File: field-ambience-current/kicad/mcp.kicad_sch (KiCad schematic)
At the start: 17 parts, among them SW1 Cell 1 (2u Choc V2 Hot-Swap), SW10 Modifier CLEAR (1u Choc V2 Ho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, SW2 Cell 2 (2u Choc V2 Hot-Swap), SW3 Cell 3 (2u Choc V2 Hot-Swap), SW4 Cell 4 (2u Choc V2 Hot-Swap), SW5 Cell 5 (2u Choc V2 Hot-Swap), SW6 Modifier SHIFT (1u Choc V2 Ho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, SW7 Modifier HOLD (1u Choc V2 Hot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, SW8 Modifier DRONE (1u Choc V2 Ho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, SW9 Modifier GENERATE (1u Choc V2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

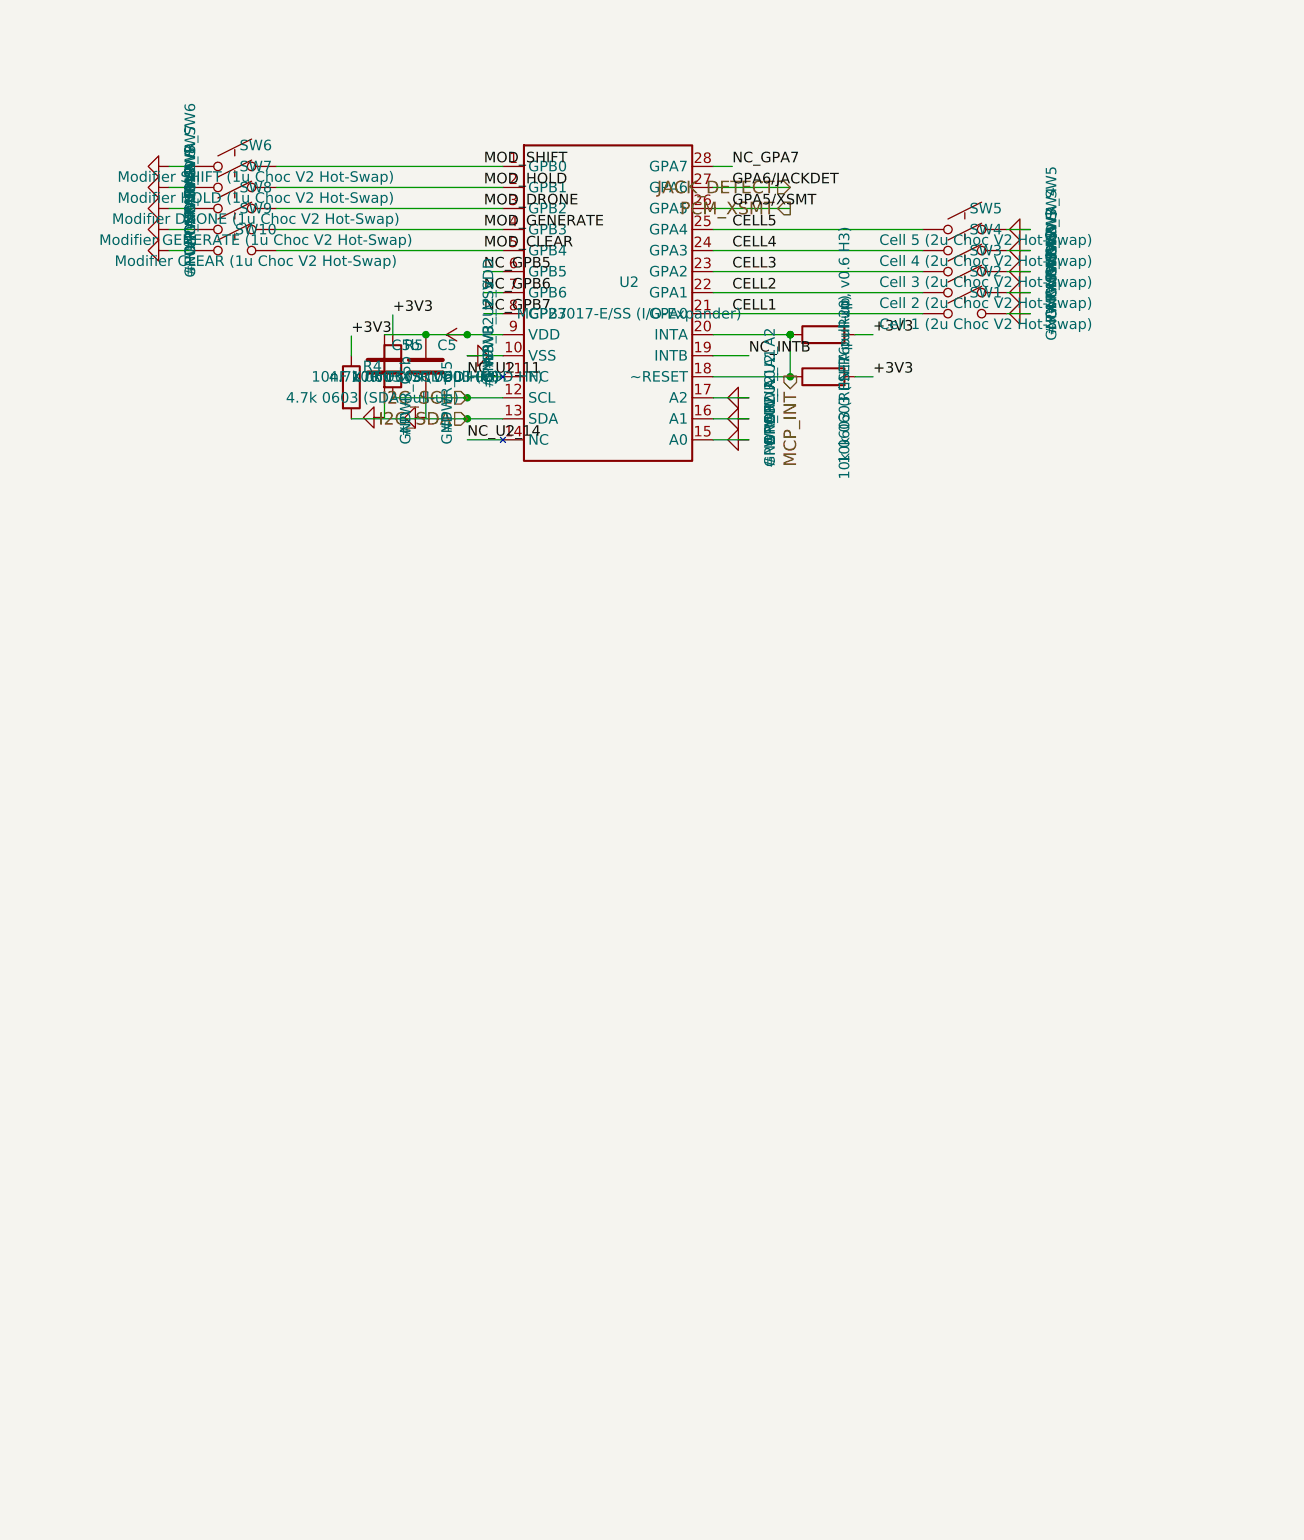
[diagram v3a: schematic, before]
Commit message: pcb(gen): r10-LED — KiCad-Generator nachgezogen (PCA9685 + 10 LEDs + SW-MPN-Swap)
Erste Hälfte von r10-B9/r7-B3 (Generator-Update). Schließt die r10-LED-Lücke
zwischen SPEC (committed in 3a10761) und KiCad-Schematic-Output.

SPEC-Fix (parallel): PCA9685 EXTCLK Pin 25 von "NC" auf "GND". NXP-Datasheet
Rev 4 S.7 Footnote [2] schreibt explizit Ground vor wenn unused — wäre latenter
Bug (undefined HF-Pickup, Oscillator-Destabilisierung). Datasheet via WebFetch
+ PDF-Read verifiziert.

Generator-Änderungen in generate_kicad_project.py:
- NEU `_pca9685pw_lib_symbol()` (TSSOP-28, alle 28 Pins per NXP-Datasheet)
  + LIB_SYMBOLS-Composition-Append
- SW6-SW10 Footprint/MPN-Swap: Kailh Choc V2 Hot-Swap → Button_Switch_SMD:
  SW_SPST_TL3342, MPN HX 12x12x7.3TPFT-B, LCSC C36498966 (r10)
- mcp_sheet() erweitert mit komplettem PCA9685-Block:
  - U6 PCA9685PW @ (130, 165), Body y=148..182 (40mm unter U2)
  - A0-A5 → GND (Adresse 0x40)
  - VSS/VDD → GND/+3V3
  - SDA/SCL → I2C_SDA/I2C_SCL (Same-Name-Match mit MCP-Bus)
  - C_PCA_VDD 10µF + C_PCA_VDD_HF 100nF Decoupling am VDD
  - R_OE 10kΩ Pull-Up zu +3V3 (default disabled)
  - EXTCLK → GND (per Datasheet, NICHT NC)
  - 10× LED+R Pairs in 5×2 Grid (y=200, y=215):
    * LED6-LED10 (Modifier) auf PCA-Ch 0-4
    * LED11-LED15 (Cell-HOLD) auf PCA-Ch 5-9
    * Net-Label-Matching von PCA-LED-pin zu LED-Kathode (LED6_K..LED15_K)
  - LED10-LED15 (PCA-Ch 10-15) als NC_PCA_LEDn (LED10 wird r12 = STATUS)

LIB_SYMBOLS-Block wird in jedes Sheet inlined → audio/encoder/oled/pico/
power_tree.kicad_sch erhalten je 95 Zeilen PCA9685-Symbol-Definition (KiCad-
Standard-Verfahren, kein Duplikat-Konflikt da nur ein Sheet U6 platziert).

mcp.kicad_sch wuchs 800 → 2810 Zeilen (+1142 für U6-Cluster).

Smoke-Tests:
- Generator läuft fehlerfrei
- 8192 öffnende = 8192 schließende Parens (balanced)
- Alle erwarteten lib_ids vorhanden (Device:C/R/LED, Driver_LED:PCA9685PW, ...)
- LED6-LED15 + R_LED6-R_LED15 alle generiert

KiCad-GUI-ERC verbleibt User-Schritt (ke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
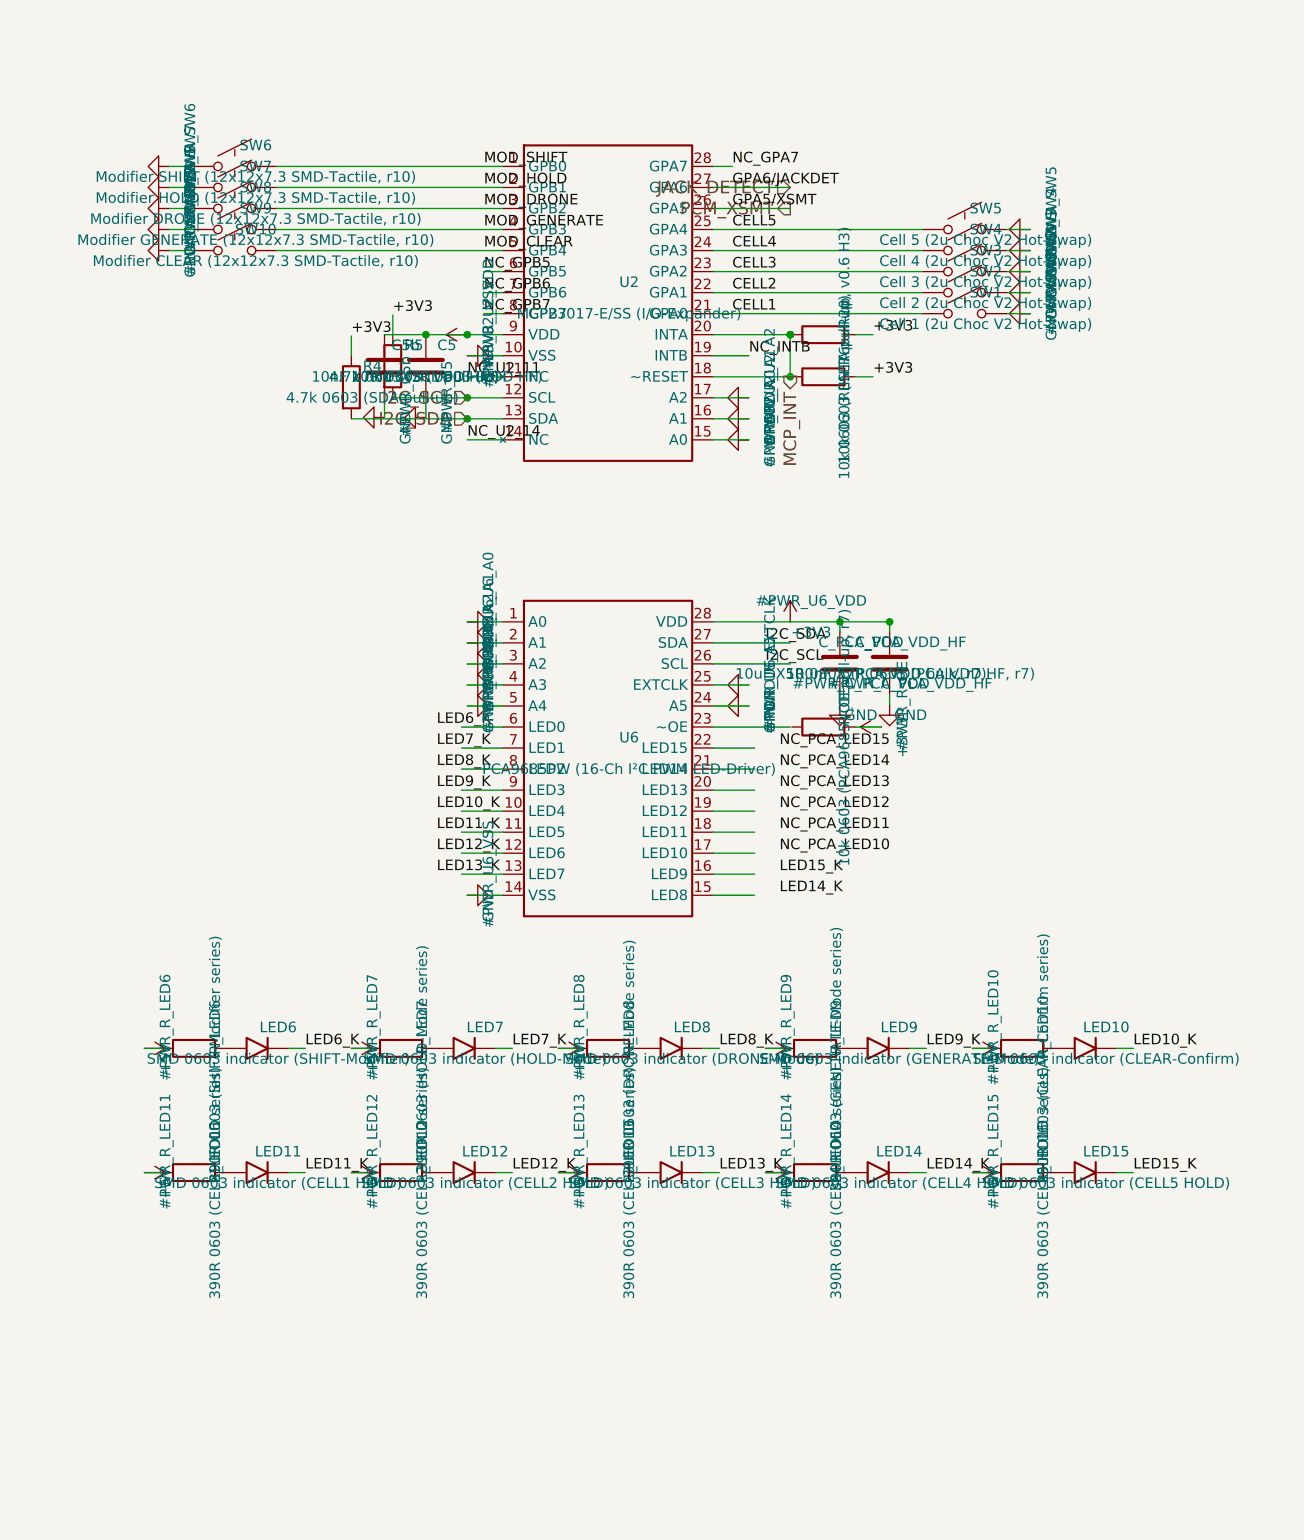
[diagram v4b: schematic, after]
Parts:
- added C_PCA_VDD: 10uF X5R 0805 (PCA VDD bulk, r7), Capacitor_SMD:C_0805_2012Metric, symbol Device:C
- added C_PCA_VDD_HF: 100nF X7R 0603 (PCA VDD HF, r7), Capacitor_SMD:C_0603_1608Metric, symbol Device:C
- added LED10: SMD 0603 indicator (CLEAR-Confirm), LED_SMD:LED_0603_1608Metric, symbol Device:LED
- added LED11: SMD 0603 indicator (CELL1 HOLD), LED_SMD:LED_0603_1608Metric, symbol Device:LED
- added LED12: SMD 0603 indicator (CELL2 HOLD), LED_SMD:LED_0603_1608Metric, symbol Device:LED
- added LED13: SMD 0603 indicator (CELL3 HOLD), LED_SMD:LED_0603_1608Metric, symbol Device:LED
- added LED14: SMD 0603 indicator (CELL4 HOLD), LED_SMD:LED_0603_1608Metric, symbol Device:LED
- added LED15: SMD 0603 indicator (CELL5 HOLD), LED_SMD:LED_0603_1608Metric, symbol Device:LED
- added LED6: SMD 0603 indicator (SHIFT-Modifier), LED_SMD:LED_0603_1608Metric, symbol Device:LED
- added LED7: SMD 0603 indicator (HOLD-Mode), LED_SMD:LED_0603_1608Metric, symbol Device:LED
- added LED8: SMD 0603 indicator (DRONE-Mode), LED_SMD:LED_0603_1608Metric, symbol Device:LED
- added LED9: SMD 0603 indicator (GENERATE-Mode), LED_SMD:LED_0603_1608Metric, symbol Device:LED
- added R_LED10: 390R 0603 (CLEAR-Confirm series), Resistor_SMD:R_0603_1608Metric, symbol Device:R
- added R_LED11: 390R 0603 (CELL1 HOLD series), Resistor_SMD:R_0603_1608Metric, symbol Device:R
- added R_LED12: 390R 0603 (CELL2 HOLD series), Resistor_SMD:R_0603_1608Metric, symbol Device:R
- added R_LED13: 390R 0603 (CELL3 HOLD series), Resistor_SMD:R_0603_1608Metric, symbol Device:R
- added R_LED14: 390R 0603 (CELL4 HOLD series), Resistor_SMD:R_0603_1608Metric, symbol Device:R
- added R_LED15: 390R 0603 (CELL5 HOLD series), Resistor_SMD:R_0603_1608Metric, symbol Device:R
- added R_LED6: 390R 0603 (SHIFT-Modifier series), Resistor_SMD:R_0603_1608Metric, symbol Device:R
- added R_LED7: 390R 0603 (HOLD-Mode series), Resistor_SMD:R_0603_1608Metric, symbol Device:R
- added R_LED8: 390R 0603 (DRONE-Mode series), Resistor_SMD:R_0603_1608Metric, symbol Device:R
- added R_LED9: 390R 0603 (GENERATE-Mode series), Resistor_SMD:R_0603_1608Metric, symbol Device:R
- added R_OE: 10k 0603 (PCA9685 /OE pull-up, r7), Resistor_SMD:R_0603_1608Metric, symbol Device:R
- added U6: PCA9685PW (16-Ch I²C PWM LED-Driver), Package_SO:TSSOP-28_4.4x9.7mm_P0.65mm, symbol Driver_LED:PCA9685PW
- SW10: value Modifier CLEAR (1u Choc V2 Hot-Swap) -> Modifier CLEAR (12x12x7.3 SMD-Tactile, r10); footprint Switch_Keyboard_Hotswap_Kailh:SW_Hotswap_Kailh_Choc_V1V2_1.00u -> Button_Switch_SMD:SW_SPST_TL3342; LCSC TBD (separat bestellen) -> C36498966; MPN Kailh Choc V2 hot-swap socket -> HX 12x12x7.3TPFT-B
- SW6: value Modifier SHIFT (1u Choc V2 Hot-Swap) -> Modifier SHIFT (12x12x7.3 SMD-Tactile, r10); footprint Switch_Keyboard_Hotswap_Kailh:SW_Hotswap_Kailh_Choc_V1V2_1.00u -> Button_Switch_SMD:SW_SPST_TL3342; LCSC TBD (separat bestellen) -> C36498966; MPN Kailh Choc V2 hot-swap socket -> HX 12x12x7.3TPFT-B
- SW7: value Modifier HOLD (1u Choc V2 Hot-Swap) -> Modifier HOLD (12x12x7.3 SMD-Tactile, r10); footprint Switch_Keyboard_Hotswap_Kailh:SW_Hotswap_Kailh_Choc_V1V2_1.00u -> Button_Switch_SMD:SW_SPST_TL3342; LCSC TBD (separat bestellen) -> C36498966; MPN Kailh Choc V2 hot-swap socket -> HX 12x12x7.3TPFT-B
- SW8: value Modifier DRONE (1u Choc V2 Hot-Swap) -> Modifier DRONE (12x12x7.3 SMD-Tactile, r10); footprint Switch_Keyboard_Hotswap_Kailh:SW_Hotswap_Kailh_Choc_V1V2_1.00u -> Button_Switch_SMD:SW_SPST_TL3342; LCSC TBD (separat bestellen) -> C36498966; MPN Kailh Choc V2 hot-swap socket -> HX 12x12x7.3TPFT-B
- SW9: value Modifier GENERATE (1u Choc V2 Hot-Swap) -> Modifier GENERATE (12x12x7.3 SMD-Tactile, r10); footprint Switch_Keyboard_Hotswap_Kailh:SW_Hotswap_Kailh_Choc_V1V2_1.00u -> Button_Switch_SMD:SW_SPST_TL3342; LCSC TBD (separat bestellen) -> C36498966; MPN Kailh Choc V2 hot-swap socket -> HX 12x12x7.3TPFT-B
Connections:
- net +3V3: now also C_PCA_VDD.1, C_PCA_VDD_HF.1, R_OE.2, U6.28 (VDD)
- net GND: now also C_PCA_VDD.2, C_PCA_VDD_HF.2, U6.1 (A0), U6.14 (VSS), U6.2 (A1), U6.24 (A5), U6.25 (EXTCLK), U6.3 (A2), U6.4 (A3), U6.5 (A4)
- net I2C_SCL: now also U6.26 (SCL)
- net I2C_SDA: now also U6.27 (SDA)
- new net: LED10.2 (A), R_LED10.2
- new net: LED7.2 (A), R_LED7.2
- new net: LED6.2 (A), R_LED6.2
- new net: LED15.2 (A), R_LED15.2
- new net: LED13.2 (A), R_LED13.2
- new net: LED14.2 (A), R_LED14.2
- new net: LED11.2 (A), R_LED11.2
- new net: LED8.2 (A), R_LED8.2
- new net: LED12.2 (A), R_LED12.2
- new net: LED9.2 (A), R_LED9.2
- new net +5V: R_LED10.1, R_LED11.1, R_LED12.1, R_LED13.1, R_LED14.1, R_LED15.1, R_LED6.1, R_LED7.1, R_LED8.1, R_LED9.1
- new net LED10_K: LED10.1 (K)
- new net LED11_K: LED11.1 (K)
- new net LED12_K: LED12.1 (K)
- new net LED13_K: LED13.1 (K)
- new net LED14_K: LED14.1 (K)
- new net LED15_K: LED15.1 (K)
- new net LED6_K: LED6.1 (K)
- new net LED7_K: LED7.1 (K)
- new net LED8_K: LED8.1 (K)
- new net LED9_K: LED9.1 (K)
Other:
- title: Field Ambience PCB — Sheet 4: MCP23017 + 10 Switches -> Field Ambience PCB — Sheet 4: MCP23017 + PCA9685 + 10 Switches + 10 LEDs
